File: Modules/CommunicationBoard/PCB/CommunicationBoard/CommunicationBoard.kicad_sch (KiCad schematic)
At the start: 11 parts, among them J1 CIO_MAIN_CONNECTOR, J2 Conn_Coaxial, U1 SX1278

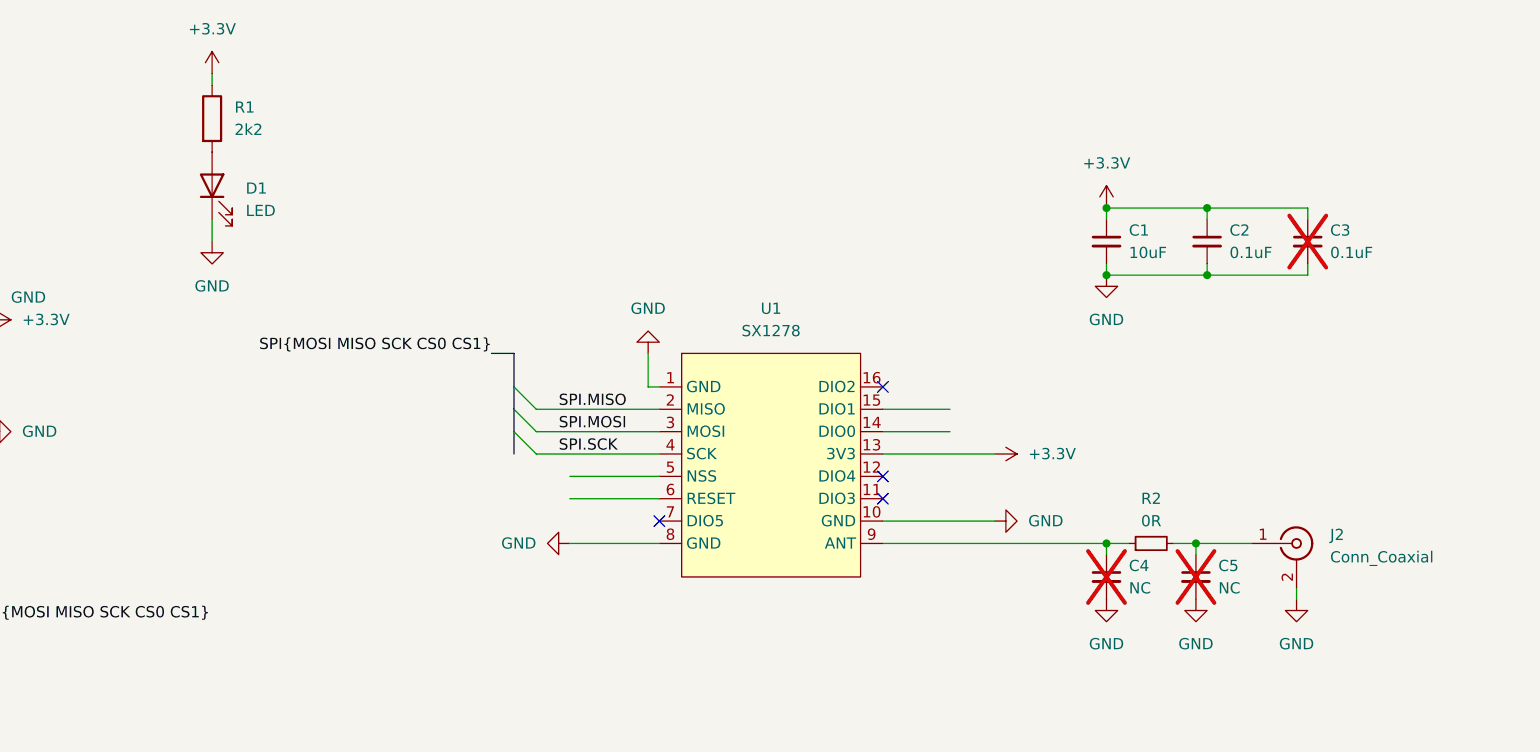
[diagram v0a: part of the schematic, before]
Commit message: Update Communication Board with E22-900M30S module
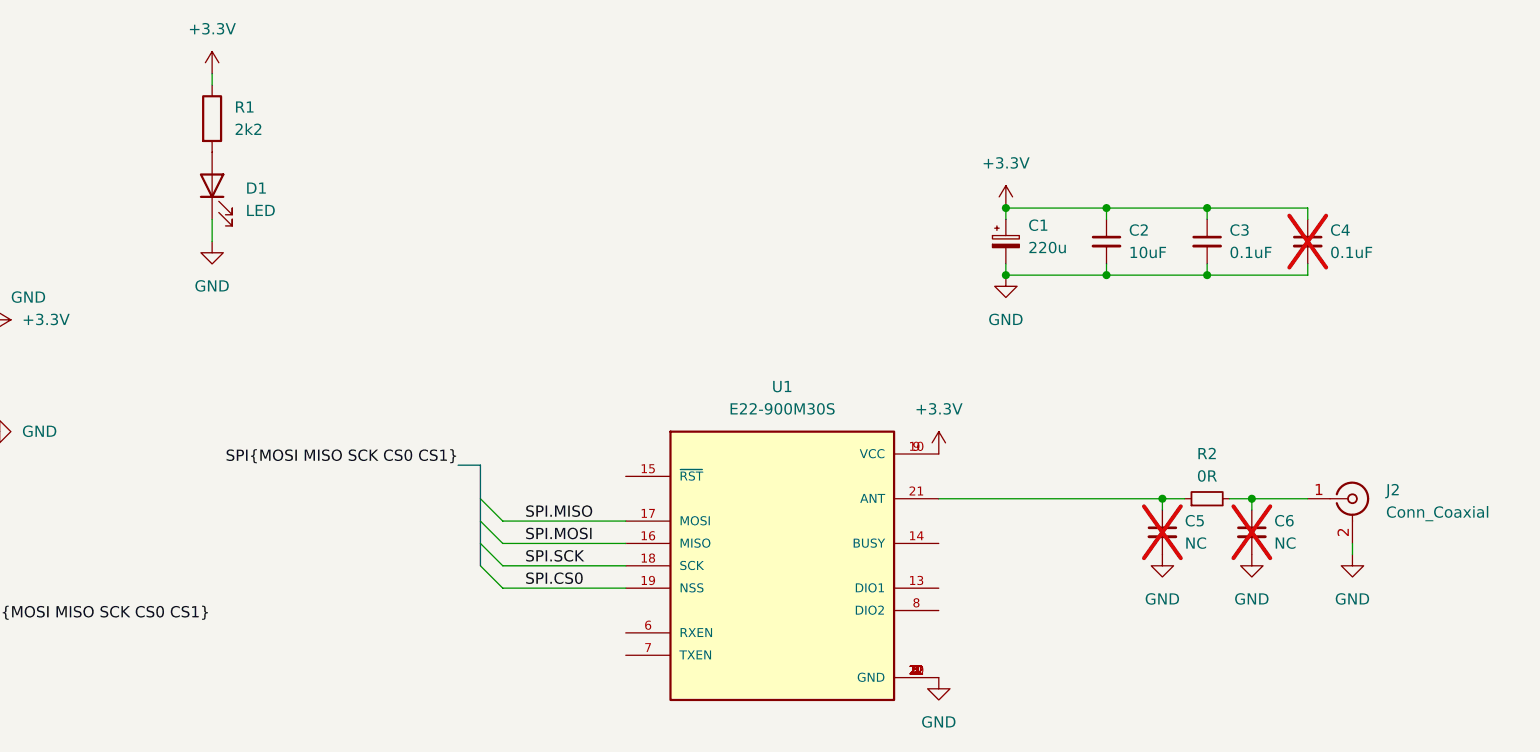
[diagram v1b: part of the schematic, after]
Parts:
- removed U1: SX1278, IcaroFootprints:SX1278 MODULE, symbol IcaroLib:SX1278
- added C1: 220u, Capacitor_Tantalum_SMD:CP_EIA-3528-21_Kemet-B_Pad1.50x2.35mm_HandSolder, symbol Device:C_Polarized_Small
- added U1: E22-900M30S, IcaroFootprints:XCVR_E22-900M30S, symbol IcaroLib:E22-900M30S
- renumbered C1 to C2, C2 to C3, C3 to C4, C4 to C5, C5 to C6
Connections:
- net +3.3V: now also C1.1, U1.10 (VCC), U1.9 (VCC)
- net GND: now also C1.2, U1.1 (GND), U1.11 (GND), U1.12 (GND), U1.2 (GND), U1.20 (GND), U1.22 (GND), U1.3 (GND), U1.4 (GND), U1.5 (GND)
- net SPI.CS0: now also U1.19 (NSS)
- net SPI.MISO: now also U1.17 (MOSI)
- net SPI.MOSI: now also U1.16 (MISO)
- net SPI.SCK: now also U1.18 (SCK)
- net at C5.1, R2.1: now also U1.21 (ANT)
- no-connect marks 17 -> 13
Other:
- moved on the sheet: C5, C6, J2, R2

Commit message: First PCB layout version
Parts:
- added JP1, JP2, JP3, JP4: SolderJumper_2_Bridged, Jumper:SolderJumper-2_P1.3mm_Bridged_RoundedPad1.0x1.5mm, symbol Jumper:SolderJumper_2_Bridged
- added TP1, TP2: TestPoint, TestPoint:TestPoint_Pad_D2.5mm, symbol Connector:TestPoint
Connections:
- net DIO1: now reaches U1.13 (DIO1)
- net DIO1: now also TP1.1
- net BUSY: now reaches U1.14 (BUSY)
- net BUSY: now also JP2.2 (B)
- net ~{RST}: now reaches U1.15 (~{RST})
- net ~{RST}: now also JP1.2 (B)
- net RXEN: now reaches U1.6 (RXEN)
- net RXEN: now also JP3.2 (B)
- net TXEN: now reaches U1.7 (TXEN)
- net TXEN: now also JP4.2 (B)
- net DIO2: now reaches U1.8 (DIO2)
- net DIO2: now also TP2.1
- net IO0: now reaches J1.11 (IO0)
- net IO0: now also JP1.1 (A)
- net IO1: now reaches J1.12 (IO1)
- net IO1: now also JP2.1 (A)
- net IO2: now reaches J1.13 (IO2)
- net IO2: now also JP3.1 (A)
- net IO3: now reaches J1.14 (IO3)
- net IO3: now also JP4.1 (A)
- net SPI.CS1: no longer names the net of J1.23 (CS1)
- no-connect marks 13 -> 10
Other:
- note added: "3V3 Power"
- note added: "3V3 Power LED"
- note added: "IO Connector"
- note added: "LoRa Communication"
- note added: "Test Solder"
- moved on the sheet: C1, C2, C3, C4, C5, C6, D1, J1, J2, R1, R2, U1

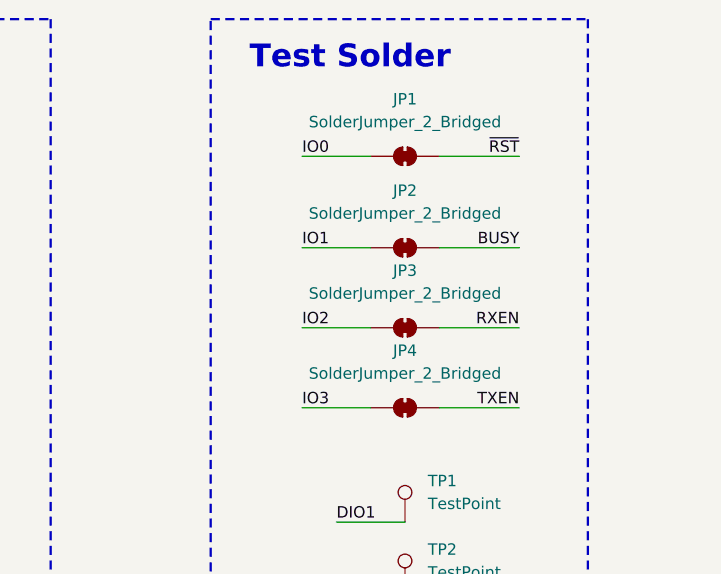
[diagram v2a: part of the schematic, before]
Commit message: Change solder jumper from close to open
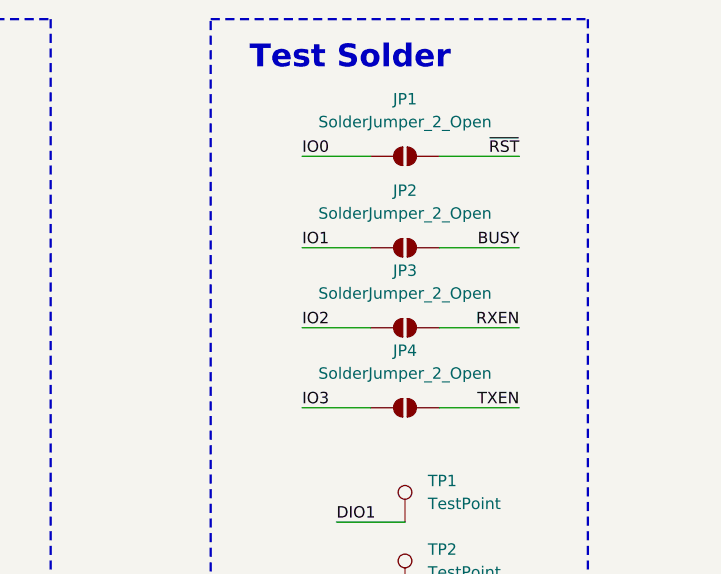
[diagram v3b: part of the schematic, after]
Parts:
- removed JP1, JP2, JP3, JP4: SolderJumper_2_Bridged, Jumper:SolderJumper-2_P1.3mm_Bridged_RoundedPad1.0x1.5mm, symbol Jumper:SolderJumper_2_Bridged
- added JP1, JP2, JP3, JP4: SolderJumper_2_Open, Jumper:SolderJumper-2_P1.3mm_Open_RoundedPad1.0x1.5mm, symbol Jumper:SolderJumper_2_Open
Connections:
- net BUSY: now also JP2.2 (B)
- net IO0: now also JP1.1 (A)
- net IO1: now also JP2.1 (A)
- net IO2: now also JP3.1 (A)
- net IO3: now also JP4.1 (A)
- net RXEN: now also JP3.2 (B)
- net TXEN: now also JP4.2 (B)
- net ~{RST}: now also JP1.2 (B)

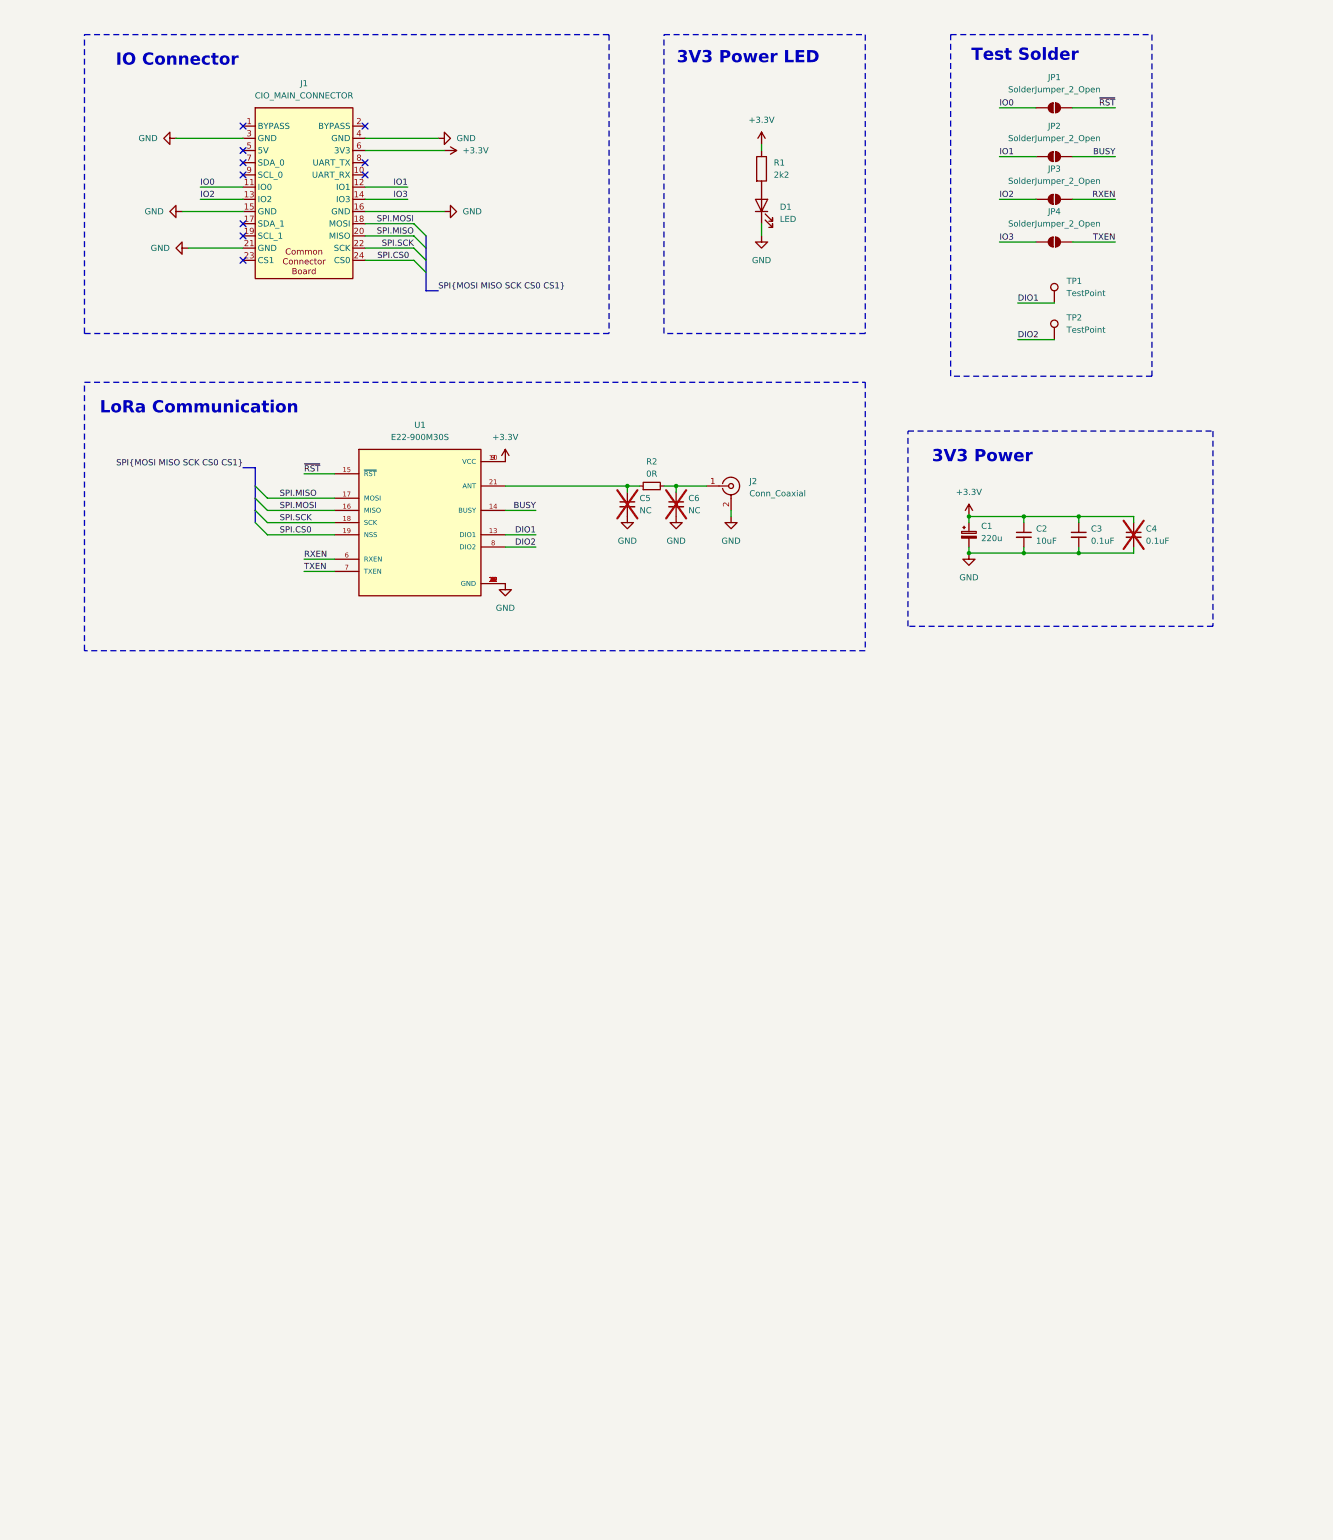
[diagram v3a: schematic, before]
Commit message: First PCBA with ESP32
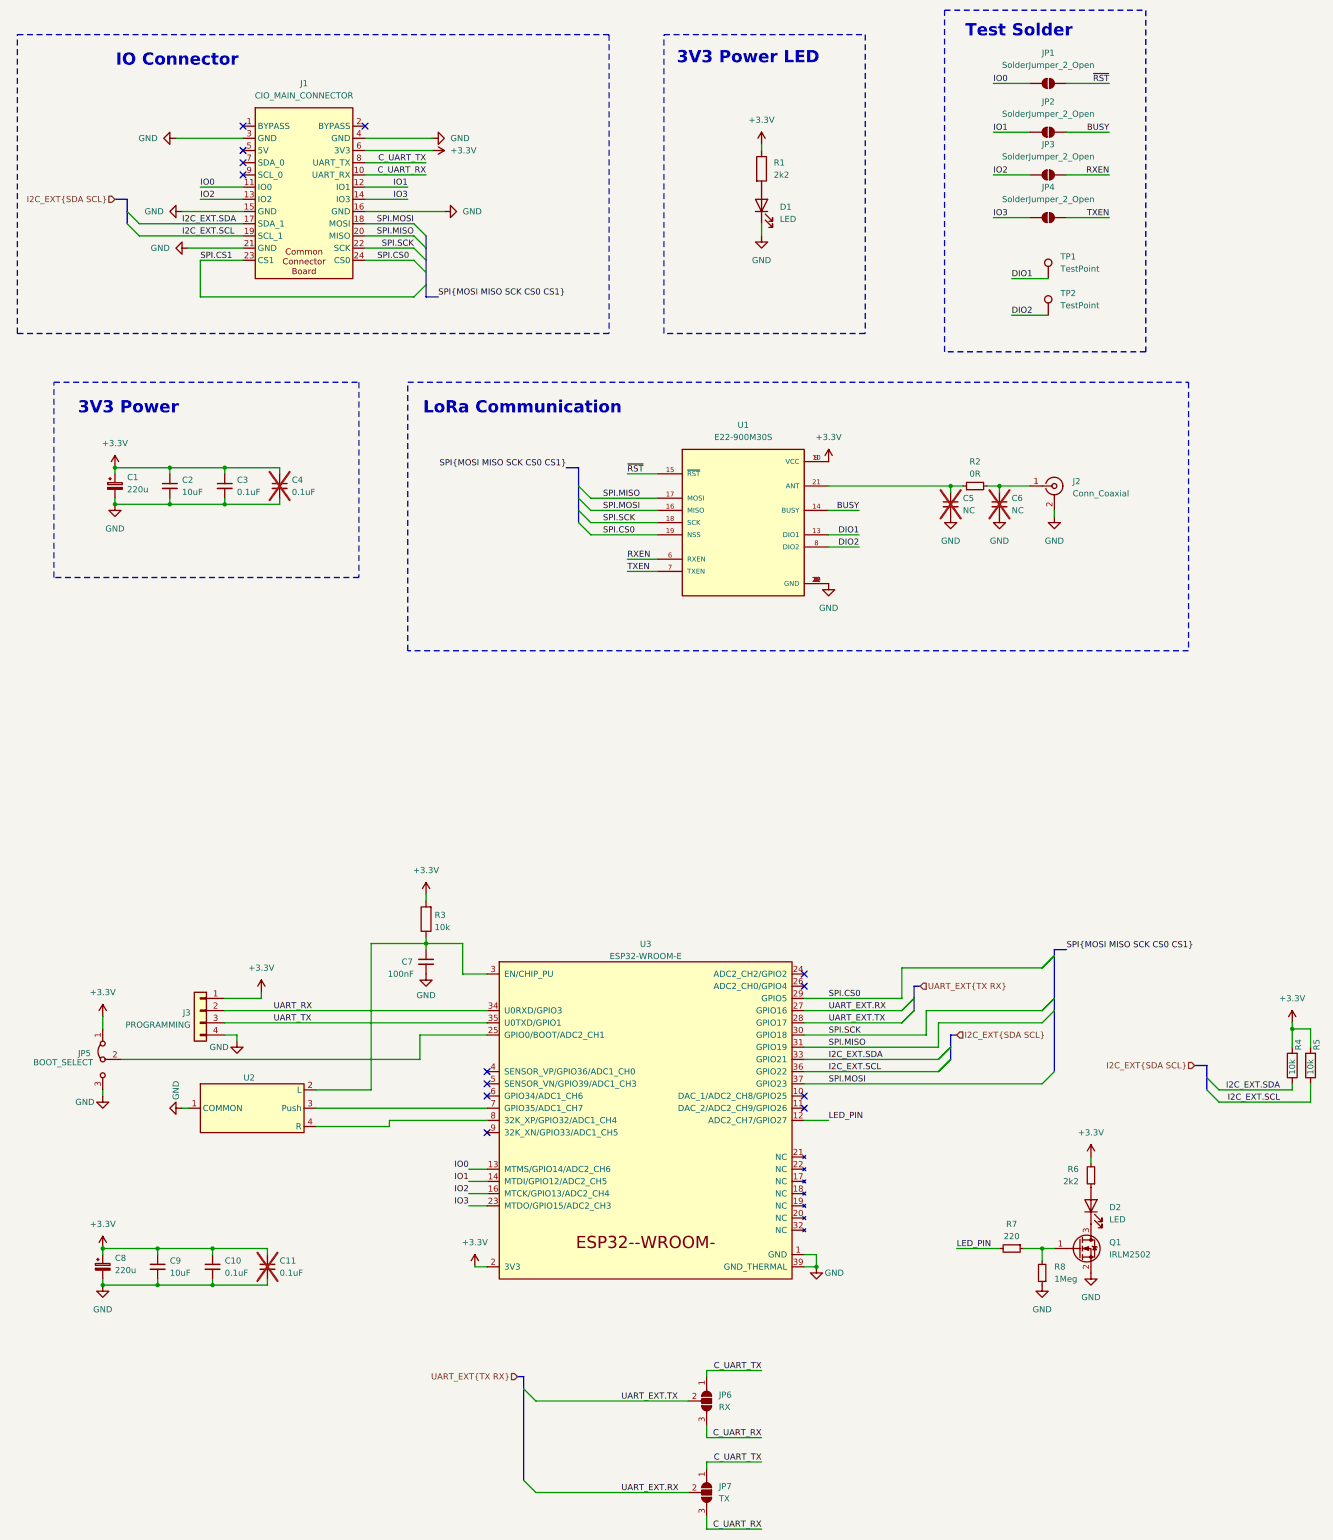
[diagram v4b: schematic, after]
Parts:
- added C10, C11: 0.1uF, Capacitor_SMD:C_0603_1608Metric_Pad1.08x0.95mm_HandSolder, symbol Device:C_Small
- added C7: 100nF, Capacitor_SMD:C_0603_1608Metric_Pad1.08x0.95mm_HandSolder, symbol Device:C_Small
- added C8: 220u, Capacitor_Tantalum_SMD:CP_EIA-3528-21_Kemet-B_Pad1.50x2.35mm_HandSolder, symbol Device:C_Polarized_Small
- added C9: 10uF, Capacitor_SMD:C_0603_1608Metric_Pad1.08x0.95mm_HandSolder, symbol Device:C_Small
- added D2: LED, LED_SMD:LED_0805_2012Metric_Pad1.15x1.40mm_HandSolder, symbol Device:LED
- added J3: PROGRAMMING, Connector_PinHeader_2.54mm:PinHeader_1x04_P2.54mm_Vertical, symbol Connector_Generic:Conn_01x04
- added JP5: BOOT_SELECT, Connector_PinHeader_2.54mm:PinHeader_1x03_P2.54mm_Vertical, symbol Jumper:Jumper_3_Bridged12
- added JP6: RX, Jumper:SolderJumper-3_P1.3mm_Open_Pad1.0x1.5mm, symbol Jumper:SolderJumper_3_Open
- added JP7: TX, Jumper:SolderJumper-3_P1.3mm_Open_Pad1.0x1.5mm, symbol Jumper:SolderJumper_3_Open
- added Q1: IRLM2502, Package_TO_SOT_SMD:SOT-23, symbol IcaroLib:IRLM2502
- added R3, R4, R5: 10k, Resistor_SMD:R_0603_1608Metric_Pad0.98x0.95mm_HandSolder, symbol Device:R
- added R6: 2k2, Resistor_SMD:R_0603_1608Metric_Pad0.98x0.95mm_HandSolder, symbol Device:R_Small
- added R7: 220, Resistor_SMD:R_0603_1608Metric_Pad0.98x0.95mm_HandSolder, symbol Device:R_Small
- added R8: 1Meg, Resistor_SMD:R_0603_1608Metric_Pad0.98x0.95mm_HandSolder, symbol Device:R_Small
- added U2: ~, IcaroFootprints:WheelSwitch, symbol IcaroLib:wheelSwitch
- added U3: ESP32-WROOM-E, RF_Module:ESP32-WROOM-32UE, symbol Espressif:ESP32-WROOM-E
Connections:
- net +3.3V: now also C10.1, C11.1, C8.1, C9.1, J3.1 (Pin_1), JP5.1 (A), R3.2, R4.2, R5.2, R6.2, U3.2 (3V3)
- net GND: now also C10.2, C11.2, C7.2, C8.2, C9.2, J3.4 (Pin_4), JP5.3 (B), Q1.2 (S), R8.1, U2.1 (COMMON), U3.1 (GND), U3.15 (GND), U3.38 (GND), U3.39 (GND_THERMAL)
- net IO0: now also U3.13 (MTMS/GPIO14/ADC2_CH6)
- net IO1: now also U3.14 (MTDI/GPIO12/ADC2_CH5)
- net IO2: now also U3.16 (MTCK/GPIO13/ADC2_CH4)
- net IO3: now also U3.23 (MTDO/GPIO15/ADC2_CH3)
- net SPI.CS0: now also U3.29 (GPIO5)
- net SPI.MISO: now also U3.31 (GPIO19)
- net SPI.MOSI: now also U3.37 (GPIO23)
- net SPI.SCK: now also U3.30 (GPIO18)
- net C_UART_RX: now reaches J1.10 (UART_RX)
- net C_UART_RX: now also JP6.3 (B), JP7.3 (B)
- net I2C_EXT.SDA: now reaches J1.17 (SDA_1)
- net I2C_EXT.SDA: now also R4.1, U3.33 (GPIO21)
- net I2C_EXT.SCL: now reaches J1.19 (SCL_1)
- net I2C_EXT.SCL: now also R5.1, U3.36 (GPIO22)
- net SPI.CS1: now reaches J1.23 (CS1)
- net C_UART_TX: now reaches J1.8 (UART_TX)
- net C_UART_TX: now also JP6.1 (A), JP7.1 (A)
- new net: JP5.2 (C), U3.25 (GPIO0/BOOT/ADC2_CH1)
- new net: C7.1, R3.1, U2.2 (L), U3.3 (EN/CHIP_PU)
- new net: D2.2 (A), R6.1
- new net: U2.3 (Push), U3.7 (GPIO35/ADC1_CH7)
- new net: U2.4 (R), U3.8 (32K_XP/GPIO32/ADC1_CH4)
- new net: D2.1 (K), Q1.3 (D)
- new net: Q1.1 (G), R7.1, R8.2
- new net LED_PIN: R7.2, U3.12 (ADC2_CH7/GPIO27)
- new net UART_EXT.RX: JP7.2 (C), U3.27 (GPIO16)
- new net UART_EXT.TX: JP6.2 (C), U3.28 (GPIO17)
- new net UART_RX: J3.2 (Pin_2), U3.34 (U0RXD/GPIO3)
- new net UART_TX: J3.3 (Pin_3), U3.35 (U0TXD/GPIO1)
- no-connect marks 10 -> 13
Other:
- moved on the sheet: C1, C2, C3, C4, C5, C6, J2, JP1, JP2, JP3, JP4, R2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
